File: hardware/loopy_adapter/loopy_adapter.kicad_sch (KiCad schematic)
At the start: 3 parts, among them J1 CART SLOT TOP ROW, J2 CART SLOT BOTTOM ROW, J3 Loopy_Slot

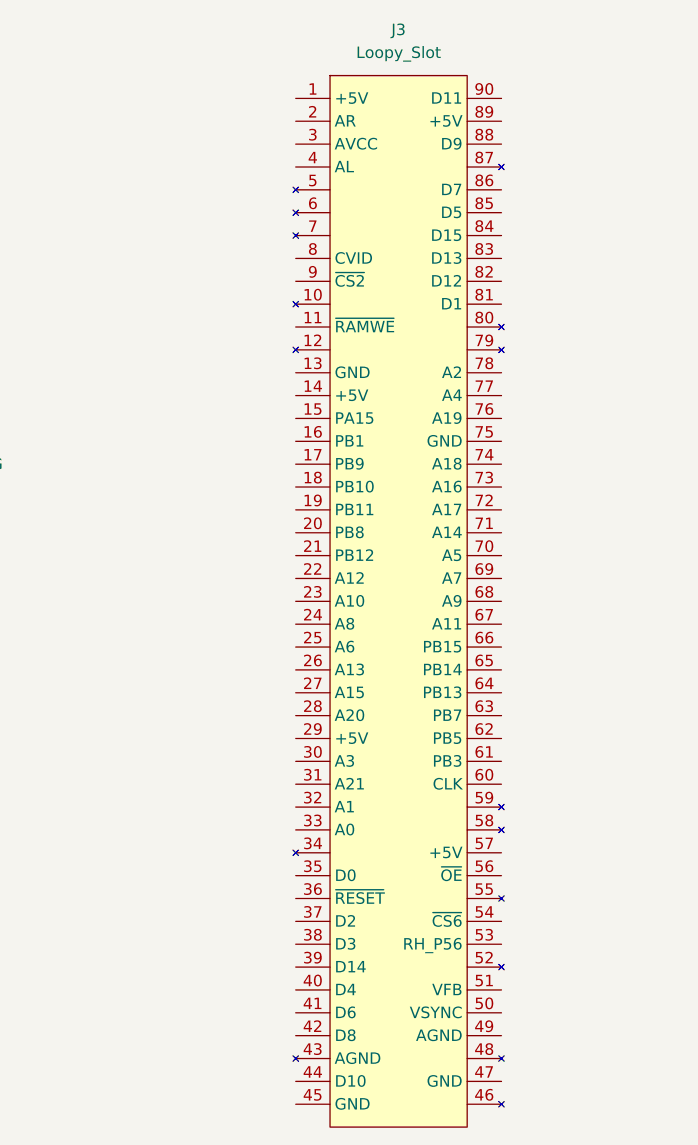
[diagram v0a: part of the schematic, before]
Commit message: Loopy adapter wired
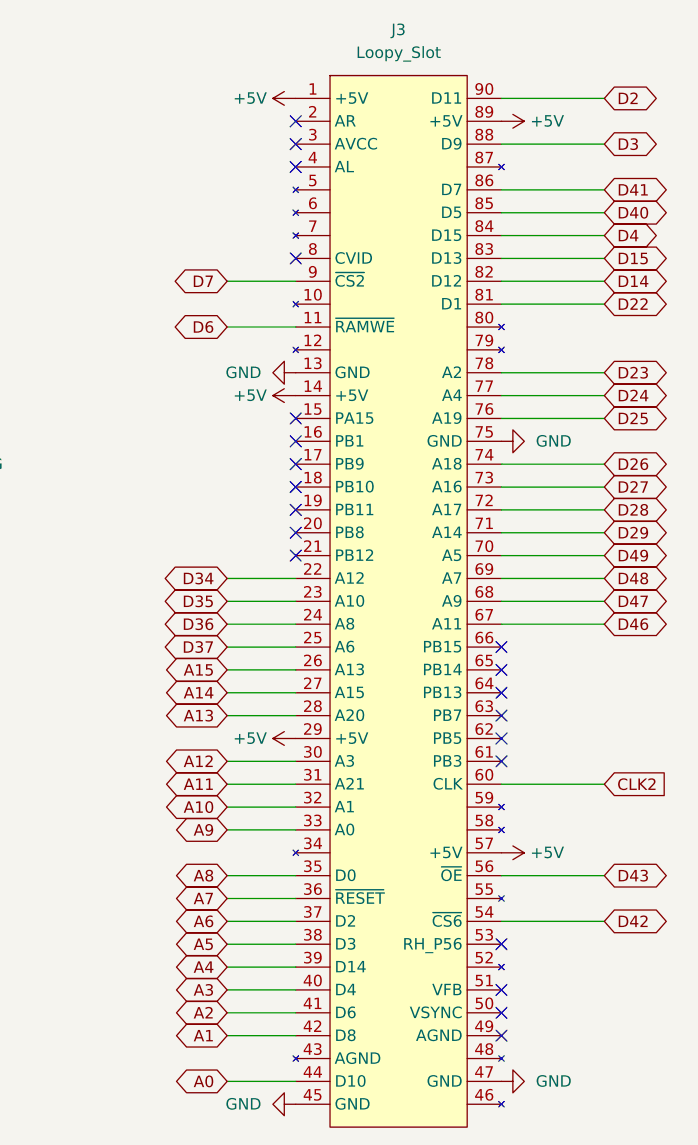
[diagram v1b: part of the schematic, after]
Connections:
- net +5V: now also J3.1 (+5V), J3.14 (+5V), J3.29 (+5V), J3.57 (+5V), J3.89 (+5V)
- net A0: now also J3.44 (D10)
- net A1: now also J3.42 (D8)
- net A10: now also J3.32 (A1)
- net A11: now also J3.31 (A21)
- net A12: now also J3.30 (A3)
- net A13: now also J3.28 (A20)
- net A14: now also J3.27 (A15)
- net A15: now also J3.26 (A13)
- net A2: now also J3.41 (D6)
- net A3: now also J3.40 (D4)
- net A4: now also J3.39 (D14)
- net A5: now also J3.38 (D3)
- net A6: now also J3.37 (D2)
- net A7: now also J3.36 (~{RESET})
- net A8: now also J3.35 (D0)
- net A9: now also J3.33 (A0)
- net CLK2: now also J3.60 (CLK)
- net D14: now also J3.82 (D12)
- net D15: now also J3.83 (D13)
- net D2: now also J3.90 (D11)
- net D22: now also J3.81 (D1)
- net D23: now also J3.78 (A2)
- net D24: now also J3.77 (A4)
- net D25: now also J3.76 (A19)
- net D26: now also J3.74 (A18)
- net D27: now also J3.73 (A16)
- net D28: now also J3.72 (A17)
- net D29: now also J3.71 (A14)
- net D3: now also J3.88 (D9)
- net D34: now also J3.22 (A12)
- net D35: now also J3.23 (A10)
- net D36: now also J3.24 (A8)
- net D37: now also J3.25 (A6)
- net D4: now also J3.84 (D15)
- net D40: now also J3.85 (D5)
- net D41: now also J3.86 (D7)
- net D42: now also J3.54 (~{CS6})
- net D43: now also J3.56 (~{OE})
- net D46: now also J3.67 (A11)
- net D47: now also J3.68 (A9)
- net D48: now also J3.69 (A7)
- net D49: now also J3.70 (A5)
- net D6: now also J3.11 (~{RAMWE})
- net D7: now also J3.9 (~{CS2})
- net GND: now also J3.13 (GND), J3.45 (GND), J3.47 (GND), J3.75 (GND)
- no-connect marks 14 -> 35
